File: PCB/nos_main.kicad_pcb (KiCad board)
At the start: 2 copper layers, 362 x 64 mm, 94 parts, among them U1 Pico_Trim, U2 ADG732BSUZ

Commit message: PCB progress 60%
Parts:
- added U3: DC/DC, nos_main:DCDC_3to5, B.Cu at (103.5, 143.6)
- moved U1 0.80 mm to (59.5, 143.3)
- moved H3 0.38 mm to (69.8, 160.2)
- moved H2 0.18 mm to (57.3, 160.2)
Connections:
- H1 pad 3: AGND -> GND
- H10 pad 3: AGND -> GND
- H11 pad 3: AGND -> GND
- H12 pad 3: AGND -> GND
- H13 pad 3: AGND -> GND
- H14 pad 3: AGND -> GND
- H15 pad 3: AGND -> GND
- H16 pad 3: AGND -> GND
- H17 pad 3: AGND -> GND
- H18 pad 3: AGND -> GND
- H19 pad 3: AGND -> GND
- H2 pad 3: AGND -> GND
- H20 pad 3: AGND -> GND
- H21 pad 3: AGND -> GND
- H22 pad 3: AGND -> GND
- H23 pad 3: AGND -> GND
- H24 pad 3: AGND -> GND
- H25 pad 3: AGND -> GND
- H26 pad 3: AGND -> GND
- H27 pad 3: AGND -> GND
- H28 pad 3: AGND -> GND
- H3 pad 3: AGND -> GND
- H4 pad 3: AGND -> GND
- H5 pad 3: AGND -> GND
- H6 pad 3: AGND -> GND
- H7 pad 3: AGND -> GND
- H8 pad 3: AGND -> GND
- H9 pad 3: AGND -> GND
- U1 pad 33: AGND -> GND
- U2 pad 41: (no net) -> unconnected-(U2-NIC-Pad41)
- U2 pad 42: (no net) -> unconnected-(U2-NIC-Pad42)
- U2 pad 44: (no net) -> unconnected-(U2-NIC-Pad44)
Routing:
- net +5V: track 0.00 -> 1377.7 mm, vias 0 -> 1
- net Vref: track 0.00 -> 541.5 mm, vias 0 -> 3
- net GND: track 0.00 -> 211.2 mm, vias 0 -> 148
- net Net-(U1-GPIO26_ADC0): track 0.00 -> 176.8 mm, vias 0 -> 1
- net +3V3: track 0.00 -> 59.4 mm
- net Net-(D10-In): track 29.8 -> 34.1 mm
- net Net-(D29-Out): track 29.8 -> 34.0 mm
- net Net-(D27-Out): track 29.8 -> 34.0 mm
- net Net-(D23-Out): track 29.8 -> 34.0 mm
- net Net-(D17-Out): track 29.8 -> 34.0 mm
- net Net-(D15-Out): track 29.8 -> 34.0 mm
- net Net-(D53-Out): track 29.8 -> 34.0 mm
- net Net-(D5-Out): track 29.8 -> 34.0 mm
- net Net-(D49-Out): track 29.8 -> 34.0 mm
- net Net-(D45-Out): track 29.8 -> 34.0 mm
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- added copper zone on B.Cu, net GND
- added copper zone on F.Cu, net GND

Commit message: PCB progress 80%
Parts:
- added C10: 0.1uF, Capacitor_SMD:C_0603_1608Metric_Pad1.08x0.95mm_HandSolder, F.Cu at (153.2, 123.8)
- added C11: 0.1uF, Capacitor_SMD:C_0603_1608Metric_Pad1.08x0.95mm_HandSolder, F.Cu at (165.7, 123.8)
- added C12: 0.1uF, Capacitor_SMD:C_0603_1608Metric_Pad1.08x0.95mm_HandSolder, F.Cu at (178.2, 123.8)
- added C13: 0.1uF, Capacitor_SMD:C_0603_1608Metric_Pad1.08x0.95mm_HandSolder, F.Cu at (192.4, 129.1)
- added C14: 0.1uF, Capacitor_SMD:C_0603_1608Metric_Pad1.08x0.95mm_HandSolder, F.Cu at (203.2, 123.8)
- added C15: 0.1uF, Capacitor_SMD:C_0603_1608Metric_Pad1.08x0.95mm_HandSolder, F.Cu at (215.7, 123.8)
- added C16: 0.1uF, Capacitor_SMD:C_0603_1608Metric_Pad1.08x0.95mm_HandSolder, F.Cu at (228.2, 123.8)
- added C17: 0.1uF, Capacitor_SMD:C_0603_1608Metric_Pad1.08x0.95mm_HandSolder, F.Cu at (242.4, 129.1)
- added C18: 0.1uF, Capacitor_SMD:C_0603_1608Metric_Pad1.08x0.95mm_HandSolder, F.Cu at (253.2, 123.8)
- added C19: 0.1uF, Capacitor_SMD:C_0603_1608Metric_Pad1.08x0.95mm_HandSolder, F.Cu at (265.7, 123.8)
- added C20: 0.1uF, Capacitor_SMD:C_0603_1608Metric_Pad1.08x0.95mm_HandSolder, F.Cu at (278.2, 123.8)
- added C21: 0.1uF, Capacitor_SMD:C_0603_1608Metric_Pad1.08x0.95mm_HandSolder, F.Cu at (290.7, 123.8)
- added C22: 0.1uF, Capacitor_SMD:C_0603_1608Metric_Pad1.08x0.95mm_HandSolder, F.Cu at (303.2, 123.8)
- added C23: 0.1uF, Capacitor_SMD:C_0603_1608Metric_Pad1.08x0.95mm_HandSolder, F.Cu at (317.4, 129.1)
- added C24: 0.1uF, Capacitor_SMD:C_0603_1608Metric_Pad1.08x0.95mm_HandSolder, F.Cu at (328.2, 123.8)
- added C25: 0.1uF, Capacitor_SMD:C_0603_1608Metric_Pad1.08x0.95mm_HandSolder, F.Cu at (340.7, 123.8)
- added C26: 0.1uF, Capacitor_SMD:C_0603_1608Metric_Pad1.08x0.95mm_HandSolder, F.Cu at (353.2, 123.8)
- added C27: 0.1uF, Capacitor_SMD:C_0603_1608Metric_Pad1.08x0.95mm_HandSolder, F.Cu at (365.7, 123.8)
- added C28: 0.1uF, Capacitor_SMD:C_0603_1608Metric_Pad1.08x0.95mm_HandSolder, F.Cu at (379.9, 129.1)
- added C29: 0.1uF, Capacitor_SMD:C_0603_1608Metric_Pad1.08x0.95mm_HandSolder, F.Cu at (206.3, 182.8)
- added C30: 1nF, Capacitor_SMD:C_0603_1608Metric_Pad1.08x0.95mm_HandSolder, B.Cu at (54.9, 157.1)
- added C31: 0.1uF, Capacitor_SMD:C_0603_1608Metric_Pad1.08x0.95mm_HandSolder, F.Cu at (41.3, 158.1)
- added C32: 0.1uF, Capacitor_SMD:C_0603_1608Metric_Pad1.08x0.95mm_HandSolder, F.Cu at (53.8, 158.1)
- added C33: 0.1uF, Capacitor_SMD:C_0603_1608Metric_Pad1.08x0.95mm_HandSolder, F.Cu at (66.3, 158.1)
- added C34: 0.1uF, Capacitor_SMD:C_0603_1608Metric_Pad1.08x0.95mm_HandSolder, F.Cu at (78.8, 158.1)
- added C35: 0.1uF, Capacitor_SMD:C_0603_1608Metric_Pad1.08x0.95mm_HandSolder, F.Cu at (91.3, 158.1)
- added C36: 0.1uF, Capacitor_SMD:C_0603_1608Metric_Pad1.08x0.95mm_HandSolder, F.Cu at (103.8, 158.1)
- added C37: 0.1uF, Capacitor_SMD:C_0603_1608Metric_Pad1.08x0.95mm_HandSolder, F.Cu at (116.3, 158.1)
- added C38: 0.1uF, Capacitor_SMD:C_0603_1608Metric_Pad1.08x0.95mm_HandSolder, F.Cu at (128.8, 158.1)
- added C39: 0.1uF, Capacitor_SMD:C_0603_1608Metric_Pad1.08x0.95mm_HandSolder, F.Cu at (141.3, 158.1)
- added C40: 0.1uF, Capacitor_SMD:C_0603_1608Metric_Pad1.08x0.95mm_HandSolder, F.Cu at (153.8, 158.1)
- added C41: 0.1uF, Capacitor_SMD:C_0603_1608Metric_Pad1.08x0.95mm_HandSolder, F.Cu at (166.3, 158.1)
- added C42: 0.1uF, Capacitor_SMD:C_0603_1608Metric_Pad1.08x0.95mm_HandSolder, F.Cu at (178.8, 158.1)
- added C43: 0.1uF, Capacitor_SMD:C_0603_1608Metric_Pad1.08x0.95mm_HandSolder, F.Cu at (191.3, 158.1)
- added C44: 0.1uF, Capacitor_SMD:C_0603_1608Metric_Pad1.08x0.95mm_HandSolder, F.Cu at (203.8, 158.1)
- added C45: 0.1uF, Capacitor_SMD:C_0603_1608Metric_Pad1.08x0.95mm_HandSolder, F.Cu at (216.3, 158.1)
- added C46: 0.1uF, Capacitor_SMD:C_0603_1608Metric_Pad1.08x0.95mm_HandSolder, F.Cu at (228.8, 158.1)
- added C47: 0.1uF, Capacitor_SMD:C_0603_1608Metric_Pad1.08x0.95mm_HandSolder, F.Cu at (241.3, 158.1)
- added C48: 0.1uF, Capacitor_SMD:C_0603_1608Metric_Pad1.08x0.95mm_HandSolder, F.Cu at (253.8, 158.1)
- added C49: 0.1uF, Capacitor_SMD:C_0603_1608Metric_Pad1.08x0.95mm_HandSolder, F.Cu at (266.3, 158.1)
- added C50: 0.1uF, Capacitor_SMD:C_0603_1608Metric_Pad1.08x0.95mm_HandSolder, F.Cu at (278.8, 158.1)
- added C51: 0.1uF, Capacitor_SMD:C_0603_1608Metric_Pad1.08x0.95mm_HandSolder, F.Cu at (291.3, 158.1)
- added C52: 0.1uF, Capacitor_SMD:C_0603_1608Metric_Pad1.08x0.95mm_HandSolder, F.Cu at (303.8, 158.1)
- added C53: 0.1uF, Capacitor_SMD:C_0603_1608Metric_Pad1.08x0.95mm_HandSolder, F.Cu at (316.3, 158.1)
- added C54: 0.1uF, Capacitor_SMD:C_0603_1608Metric_Pad1.08x0.95mm_HandSolder, F.Cu at (328.8, 158.1)
- added C55: 0.1uF, Capacitor_SMD:C_0603_1608Metric_Pad1.08x0.95mm_HandSolder, F.Cu at (341.3, 158.1)
- added C56: 0.1uF, Capacitor_SMD:C_0603_1608Metric_Pad1.08x0.95mm_HandSolder, F.Cu at (353.8, 158.1)
- added C57: 0.1uF, Capacitor_SMD:C_0603_1608Metric_Pad1.08x0.95mm_HandSolder, F.Cu at (366.3, 158.1)
- added C58: 0.1uF, Capacitor_SMD:C_0603_1608Metric_Pad1.08x0.95mm_HandSolder, F.Cu at (378.8, 158.1)
- added C9: 0.1uF, Capacitor_SMD:C_0603_1608Metric_Pad1.08x0.95mm_HandSolder, F.Cu at (140.7, 123.8)
- added JP1: SolderJumper_2_Open, Jumper:SolderJumper-2_P1.3mm_Open_RoundedPad1.0x1.5mm, B.Cu at (103.1, 135.3)
- added R1: 2K, Resistor_SMD:R_0603_1608Metric_Pad0.98x0.95mm_HandSolder, B.Cu at (88.5, 152.1)
- added R2: 10K, Resistor_SMD:R_0603_1608Metric_Pad0.98x0.95mm_HandSolder, B.Cu at (88.5, 150.6)
- moved C1 217.8 mm to (40.7, 123.8), turned to 180 degrees
- moved C2 200.0 mm to (55.2, 129.1), turned to 180 degrees
- moved C3 189.9 mm to (65.7, 123.8), turned to 180 degrees
- moved C4 176.3 mm to (78.2, 123.8), turned to 180 degrees
- moved C5 146.7 mm to (90.7, 123.8), turned to 180 degrees
- moved C6 138.3 mm to (103.2, 123.8), turned to 180 degrees
- moved C7 125.8 mm to (117.4, 129.1), turned to 180 degrees
- moved C8 123.8 mm to (128.2, 123.8), turned to 180 degrees
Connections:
- U2 pad 43: Net-(U1-GPIO26_ADC0) -> Net-(U2-D)
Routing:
- net Net-(U2-D): track 0.00 -> 139.3 mm, vias 0 -> 1
- net Net-(U1-GPIO26_ADC0): track 176.8 -> 39.6 mm, vias 1 -> 0
- net +5V: track 1377.7 -> 1427.8 mm
- net Vref: track 541.5 -> 560.6 mm
- net +3V3: track 59.4 -> 69.6 mm
- net GND: track 211.2 -> 214.9 mm, vias 148 -> 194
- net /WR: track 153.1 -> 151.6 mm
- net /A4: track 158.7 -> 157.9 mm
- net /CS: track 155.5 -> 156.1 mm
- net /A3: track 159.7 -> 159.1 mm

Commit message: PCB v1.0 done
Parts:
- added C59: 0.1uF, Capacitor_SMD:C_0603_1608Metric_Pad1.08x0.95mm_HandSolder, F.Cu at (194.5, 182.9)
- added C60: 0.1uF, Capacitor_SMD:C_0603_1608Metric_Pad1.08x0.95mm_HandSolder, F.Cu at (232.5, 182.9)
- added D57: WS2812B_Unified, nos_main:WS2812B-4020_UP, F.Cu at (188.5, 173.6)
- added D58: WS2812B_Unified, nos_main:WS2812B-4020_UP, F.Cu at (189.5, 183.6)
- added D59: WS2812B_Unified, nos_main:WS2812B-4020_UP, F.Cu at (203.0, 183.6)
- added D60: WS2812B_Unified, nos_main:WS2812B-4020_UP, F.Cu at (224.0, 183.6)
- added D61: WS2812B_Unified, nos_main:WS2812B-4020_UP, F.Cu at (237.5, 183.6)
- added D62: WS2812B_Unified, nos_main:WS2812B-4020_UP, F.Cu at (238.5, 173.6)
- moved C29 1.25 mm to (207.5, 182.8)
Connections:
- U1 pad 1: unconnected-(U1-GPIO0-Pad1) -> Net-(D57-In)
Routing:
- net +5V: track 1427.8 -> 1687.6 mm, vias 1 -> 9
- net Net-(D57-In): track 0.00 -> 183.7 mm, vias 0 -> 3
- net Net-(D59-Out): track 0.00 -> 22.0 mm
- net Net-(D57-Out): track 0.00 -> 14.7 mm, vias 0 -> 2
- net Net-(D60-Out): track 0.00 -> 14.5 mm
- net Net-(D58-Out): track 0.00 -> 14.5 mm
- net Net-(D61-Out): track 0.00 -> 12.5 mm, vias 0 -> 2
- net Vref: track 560.6 -> 559.4 mm
- net GND: track 214.9 -> 214.0 mm, vias 194 -> 201
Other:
- board text added: "Nos Pico v1.0"

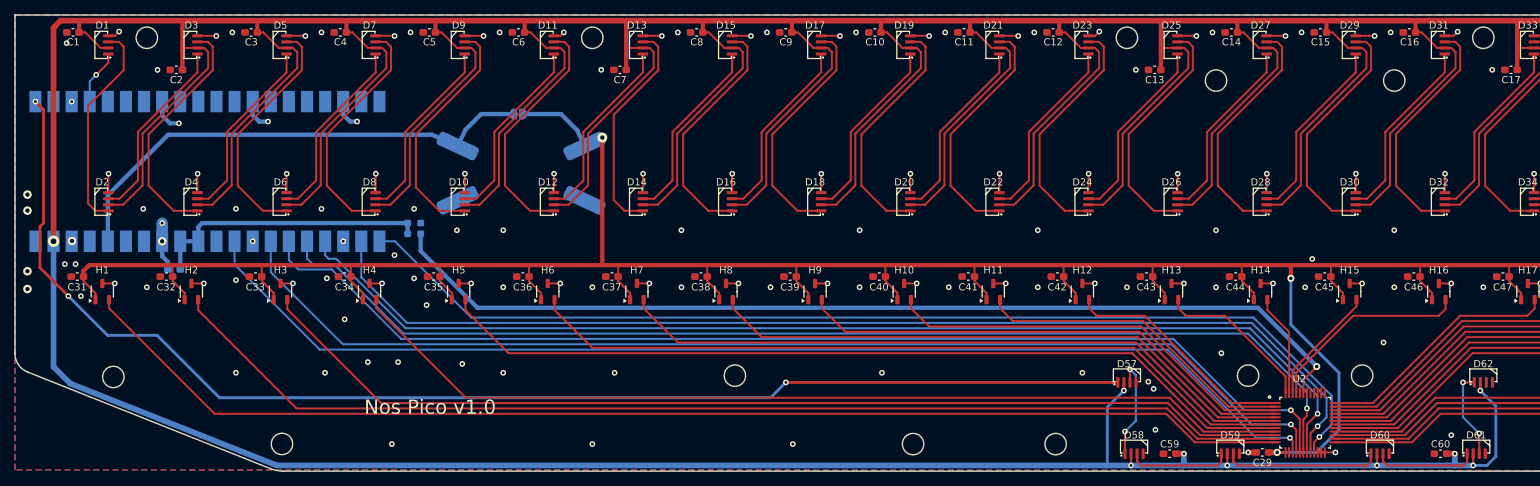
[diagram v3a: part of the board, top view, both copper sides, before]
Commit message: PCB v1.1 for dual USB port
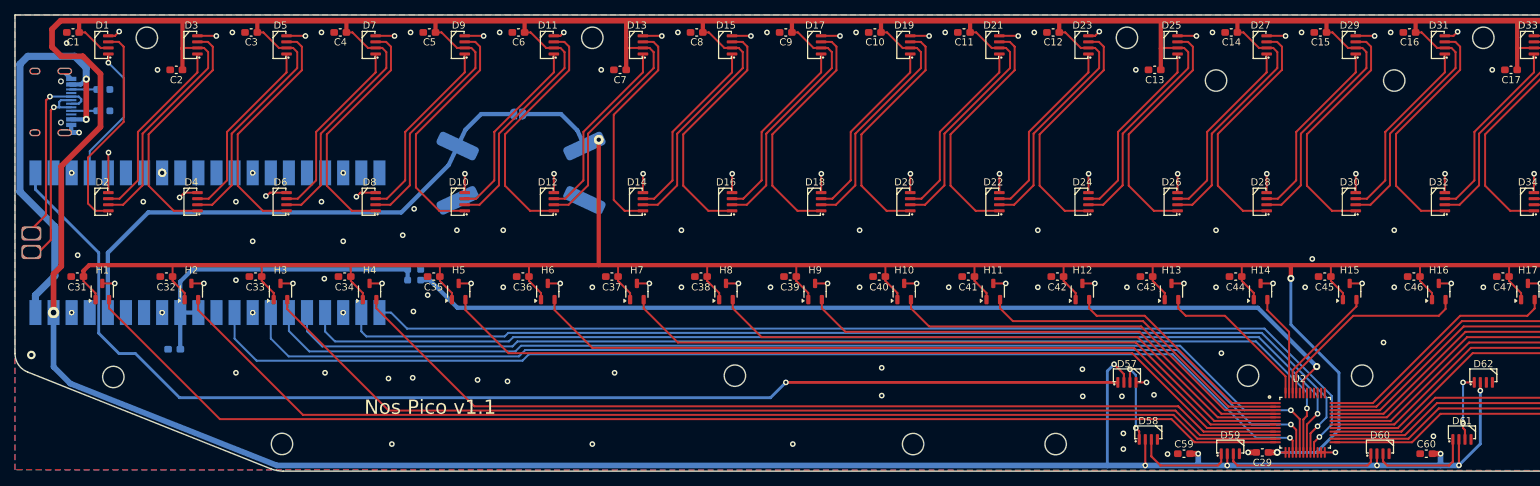
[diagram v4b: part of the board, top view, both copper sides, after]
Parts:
- added R3: 5K1, Resistor_SMD:R_0603_1608Metric_Pad0.98x0.95mm_HandSolder, B.Cu at (44.9, 134.8)
- added R4: 5K1, Resistor_SMD:R_0603_1608Metric_Pad0.98x0.95mm_HandSolder, B.Cu at (44.9, 131.8)
- added USB1: U262-161N-4BVC11, Type-C:HRO-TYPE-C-31-M-12-Assembly, B.Cu at (32.7, 133.6)
- U1: value Pico_Trim -> PiPico_No_SWD; footprint nos_main:RPi_Pico_SMD_No_USB -> nos_main:RPi_Pico_SMD_Pins_No_SWD
- moved C30 11.2 mm to (54.9, 168.3)
- moved U1 10.0 mm to (59.5, 153.3)
- moved R1 6.50 mm to (88.5, 158.6)
- moved R2 6.50 mm to (88.5, 157.1)
- moved D58 2.83 mm to (191.5, 181.6)
- moved D61 2.83 mm to (235.5, 181.6)
- moved C59 2.00 mm to (196.5, 182.9)
- moved C60 2.00 mm to (230.5, 182.9)
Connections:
- U1 pad 40: unconnected-(U1-VBUS-Pad40) -> VBUS
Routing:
- net VBUS: track 0.00 -> 60.4 mm, vias 0 -> 2
- net Net-(U1-USB1): track 0.00 -> 27.2 mm, vias 0 -> 1
- net Net-(U1-USB2): track 0.00 -> 26.9 mm, vias 0 -> 1
- net +5V: track 1687.6 -> 1699.9 mm
- net Net-(D1-In): track 7.76 -> 19.6 mm
- net Net-(D57-In): track 183.7 -> 173.8 mm, vias 3 -> 1
- net GND: track 214.0 -> 206.9 mm
- net Net-(U1-GPIO26_ADC0): track 39.6 -> 46.1 mm
- net /CS: track 156.1 -> 150.9 mm
- net +3V3: track 69.6 -> 74.4 mm
- net /WR: track 151.6 -> 147.4 mm
- net Net-(U2-D): track 139.3 -> 135.2 mm
- net /A1: track 160.5 -> 156.7 mm
- net Net-(USB1-CC2): track 0.00 -> 3.79 mm
- net Net-(USB1-CC1): track 0.00 -> 3.59 mm
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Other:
- board text added: "Nos Pico v1.1"
- board text removed: "Nos Pico v1.0"

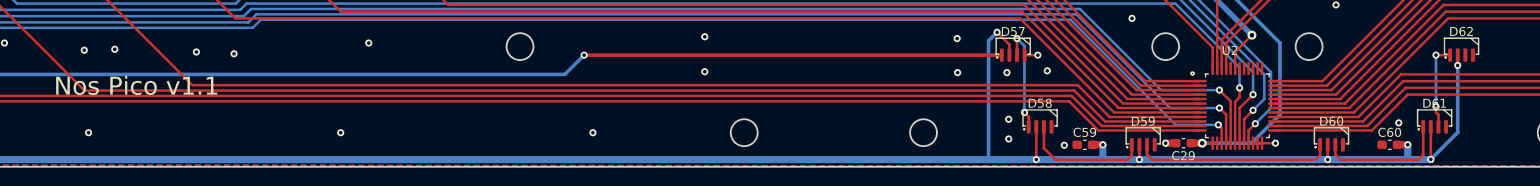
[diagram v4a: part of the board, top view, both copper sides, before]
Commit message: PCB v1.11 fix housing interference
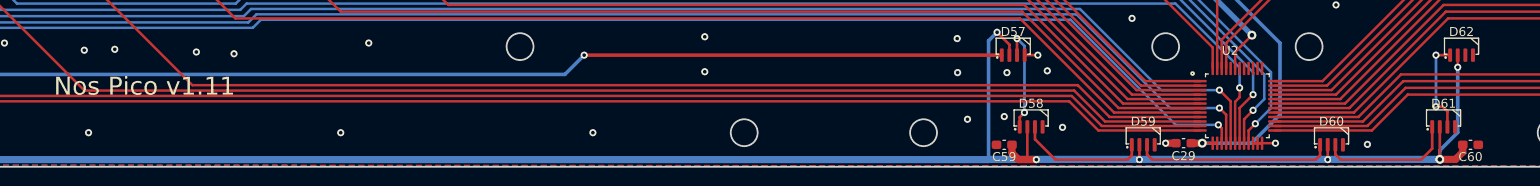
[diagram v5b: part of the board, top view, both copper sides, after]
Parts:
- moved C59 9.00 mm to (187.5, 182.9)
- moved C60 9.00 mm to (239.5, 182.9), turned to 0 degrees
- moved D58 1.00 mm to (190.5, 181.6)
- moved D61 1.00 mm to (236.5, 181.6)
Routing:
- net +5V: track 1699.9 -> 1702.5 mm, vias 9 -> 7
- net Net-(D61-Out): track 9.69 -> 10.5 mm
- net Net-(D60-Out): track 14.5 -> 15.0 mm
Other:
- board text added: "Nos Pico v1.11"
- board text removed: "Nos Pico v1.1"
